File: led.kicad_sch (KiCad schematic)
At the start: 6 parts

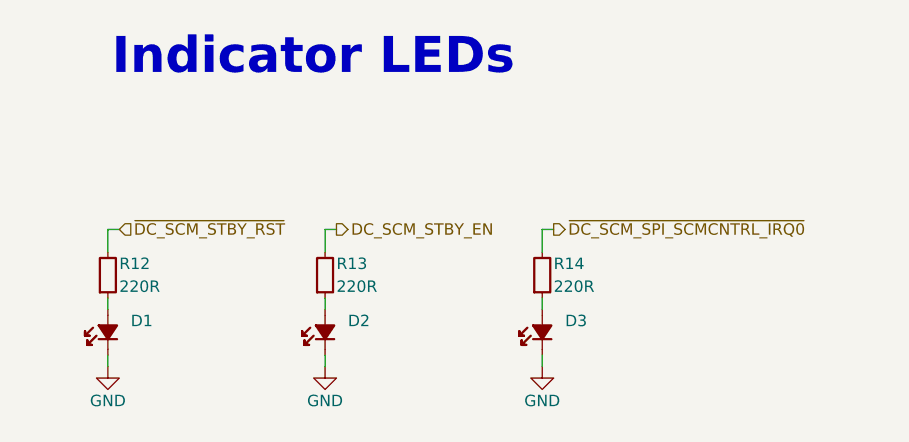
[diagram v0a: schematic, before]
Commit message: [#92504] Connect Indicator LEDs
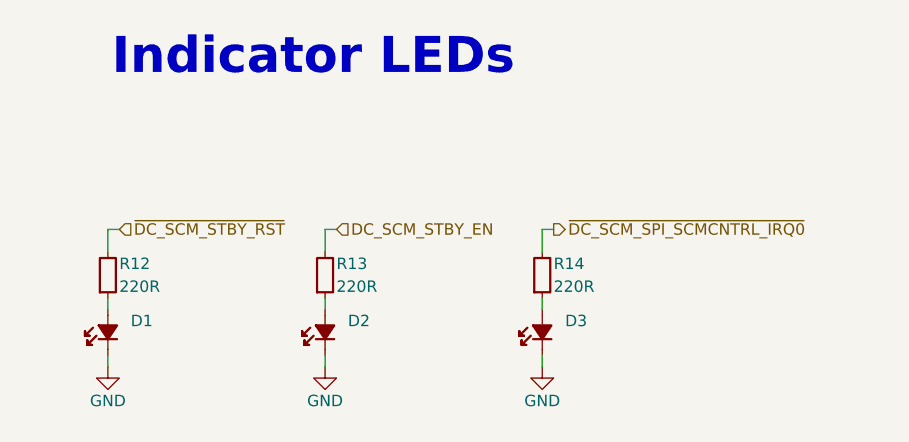
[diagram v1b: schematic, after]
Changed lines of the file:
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@@
 	)
 	(hierarchical_label "DC_SCM_STBY_EN"
-		(shape output)
+		(shape input)
 		(at 46.99 52.07 0)
 		(effects

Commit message: [#92504] Clear ERC errors
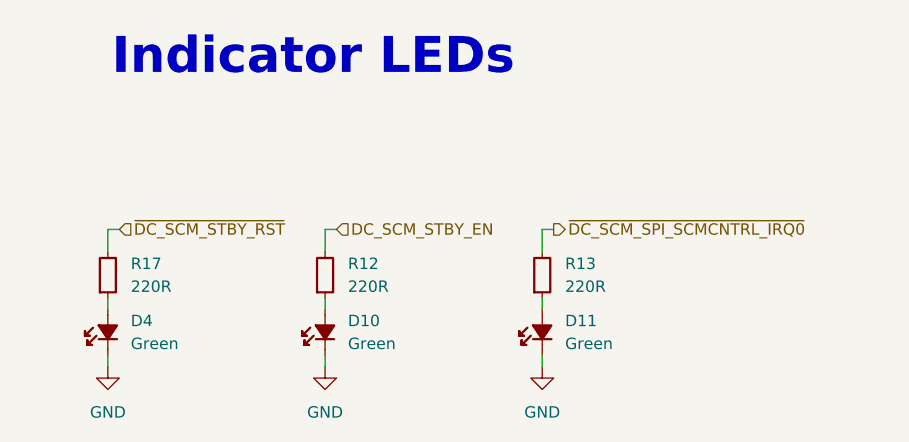
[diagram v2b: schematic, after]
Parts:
- removed D1, D2: LED_G_0402_VLMTG1500-GS08, antmicro-footprints:LED_0402_1005Metric_G, symbol antmicroLEDIndicationDiscrete:LED_G_0402_VLMTG1500-GS08
- removed D3: LED_G_0402_VLMTG1500-GS08, antmicro-footprints:LED_0402_1005Metric_B, symbol antmicroLEDIndicationDiscrete:LED_G_0402_VLMTG1500-GS08
- removed R14: R_220R_0402, antmicro-footprints:R_0402_1005Metric, symbol antmicroResistors0402:R_220R_0402
- added D10, D11, D4: LED_G_0402_VLMTG1500-GS08, antmicro-footprints:LED_0402_1005Metric_G, symbol antmicroLEDIndicationDiscrete:LED_G_0402_VLMTG1500-GS08
- added R17: R_220R_0402, antmicro-footprints:R_0402_1005Metric, symbol antmicroResistors0402:R_220R_0402
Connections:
- net DC_SCM_STBY_EN: now also R12.2; no longer R13.2
- net GND: now also D10.1 (C), D11.1 (C), D4.1 (C)
- net ~{DC_SCM_SPI_SCMCNTRL_IRQ0}: now also R13.2
- net ~{DC_SCM_STBY_RST}: now also R17.2; no longer R12.2
- net at R12.1: now also D10.2 (A)
- net at R13.1: now also D11.2 (A)
- new net: D4.2 (A), R17.1
